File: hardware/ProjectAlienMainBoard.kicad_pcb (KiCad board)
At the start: 2 copper layers, 69.1 x 100.6 mm, 15 parts, among them J1 Bumper Connector, J3 Left Motor Connector, J4 Right Motor Connector, J5 Pixels Connector, J6 Ultrasonic Connector, J7 Micro USB, J8 I2C Multiplexer, U1 4021

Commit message: Updated name to Project A.L.I.E.N. Main Board
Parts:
- moved J5 6.06 mm to (170.2, 135.9)
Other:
- outline, holes or cut-outs redrawn
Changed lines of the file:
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@@
 	)
 	(paper "A4")
+	(title_block
+		(title "A.L.I.E.N. Main Board")
+		(date "2024-08-13")
+		(rev "1.0")
+		(comment 1 "Designed By: Harry Boyd")
+	)
 	(layers
 		(0 "F.Cu" signal)
@@
 		(property ki_fp_filters "Arduino*Nano*")
 		(sheetname "Root")
-		(sheetfile "ProjectAlienArbReplacement.kicad_sch")
+		(sheetfile "ProjectAlienMainBoard.kicad_sch")
 		(attr through_hole)
 		(fp_line
@@
 		(property ki_fp_filters "Connector*:*_1x??_*")
 		(sheetname "Root")
-		(sheetfile "ProjectAlienArbReplacement.kicad_sch")
+		(sheetfile "ProjectAlienMainBoard.kicad_sch")
 		(attr through_hole)
 		(fp_line
@@
 		(property ki_fp_filters "MountingHole*Pad*")
 		(sheetname "Root")
-		(sheetfile "ProjectAlienArbReplacement.kicad_sch")
+		(sheetfile "ProjectAlienMainBoard.kicad_sch")
 		(attr exclude_from_pos_files exclude_from_bom)
 		(fp_circle
@@
 		(property ki_fp_filters "Connector*:*_1x??_*")
 		(sheetname "Root")
-		(sheetfile "ProjectAlienArbReplacement.kicad_sch")
+		(sheetfile "ProjectAlienMainBoard.kicad_sch")
 		(attr through_hole)
 		(fp_line
@@
 		)
 		(sheetname "Root")
-		(sheetfile "ProjectAlienArbReplacement.kicad_sch")
+		(sheetfile "ProjectAlienMainBoard.kicad_sch")
 		(attr through_hole)
 		(fp_line
@@
 		(property ki_fp_filters "MountingHole*Pad*")
 		(sheetname "Root")
-		(sheetfile "ProjectAlienArbReplacement.kicad_sch")
+		(sheetfile "ProjectAlienMainBoard.kicad_sch")
 		(attr exclude_from_pos_files exclude_from_bom)
 		(fp_circle
@@
 		(property ki_fp_filters "MountingHole*Pad*")
 		(sheetname "Root")
-		(sheetfile "ProjectAlienArbReplacement.kicad_sch")
+		(sheetfile "ProjectAlienMainBoard.kicad_sch")
 		(attr exclude_from_pos_files exclude_from_bom)
 		(fp_circle
@@
 		(property ki_fp_filters "DIP*W7.62mm* SOIC*3.9x9.9mm*P1.27mm* TSSOP*4.4x5mm*P0.65mm* SOIC*5.3x10.2mm*P1.27mm*")
 		(sheetname "Root")
-		(sheetfile "ProjectAlienArbReplacement.kicad_sch")
+		(sheetfile "ProjectAlienMainBoard.kicad_sch")
 		(attr through_hole)
 		(fp_line
@@
 	(footprint "Connector_PinHeader_2.54mm:PinHeader_1x03_P2.54mm_Vertical"
 		(layer "F.Cu")
-		(at 164.25 134.62)
+		(at 170.18 135.89)
 		(descr "Through hole straight pin header, 1x03, 2.54mm pitch, single row")
 		(tags "Through hole pin header THT 1x03 2.54mm single row")
@@
 		(property ki_fp_filters "Connector*:*_1x??_*")
 		(sheetname "Root")
-		(sheetfile "ProjectAlienArbReplacement.kicad_sch")
+		(sheetfile "ProjectAlienMainBoard.kicad_sch")
 		(attr through_hole)
 		(fp_line
@@
 		)
 		(sheetname "Root")
-		(sheetfile "ProjectAlienArbReplacement.kicad_sch")
+		(sheetfile "ProjectAlienMainBoard.kicad_sch")
 		(fp_rect
 			(start 13.003859 -11.74657)
@@
 		(property ki_fp_filters "MountingHole*Pad*")
 		(sheetname "Root")
-		(sheetfile "ProjectAlienArbReplacement.kicad_sch")
+		(sheetfile "ProjectAlienMainBoard.kicad_sch")
 		(attr exclude_from_pos_files exclude_from_bom)
 		(fp_circle
@@
 		(property ki_fp_filters "Connector*:*_1x??_*")
 		(sheetname "Root")
-		(sheetfile "ProjectAlienArbReplacement.kicad_sch")
+		(sheetfile "ProjectAlienMainBoard.kicad_sch")
 		(attr through_hole)
 		(fp_line
@@
 		(property ki_fp_filters "Connector*:*_1x??_*")
 		(sheetname "Root")
-		(sheetfile "ProjectAlienArbReplacement.kicad_sch")
+		(sheetfile "ProjectAlienMainBoard.kicad_sch")
 		(attr through_hole)
 		(fp_line
@@
 		(property ki_fp_filters "Connector*:*_1x??_*")
 		(sheetname "Root")
-		(sheetfile "ProjectAlienArbReplacement.kicad_sch")
+		(sheetfile "ProjectAlienMainBoard.kicad_sch")
 		(attr through_hole)
 		(fp_line
@@
 		(property ki_fp_filters "Connector*:*_1x??_*")
 		(sheetname "Root")
-		(sheetfile "ProjectAlienArbReplacement.kicad_sch")
+		(sheetfile "ProjectAlienMainBoard.kicad_sch")
 		(attr through_hole)
 		(fp_line
@@
 		)
 	)
+	(gr_arc
+		(start 173.05 148.5)
+		(mid 171.585534 152.035534)
+		(end 168.05 153.5)
+		(stroke
+			(width 0.05)
+			(type default)
+		)
+		(layer "Edge.Cuts")
+	)
 	(gr_line
-		(start 103.95 52.9)
-		(end 173.05 52.9)
+		(start 173.05 148.5)
+		(end 173.05 57.9)
 		(stroke
 			(width 0.05)
@@
 	)
 	(gr_line
-		(start 103.95 153.5)
-		(end 103.95 52.9)
+		(start 168.05 52.9)
+		(end 108.95 52.9)
 		(stroke
 			(width 0.05)
@@
 	)
 	(gr_line
-		(start 173.05 153.5)
-		(end 173.05 52.9)
+		(start 108.95 153.5)
+		(end 168.05 153.5)
+		(stroke
+			(width 0.05)
+			(type default)
+		)
+		(layer "Edge.Cuts")
+	)
+	(gr_arc
+		(start 108.95 153.5)
+		(mid 105.414466 152.035534)
+		(end 103.95 148.5)
+		(stroke
+			(width 0.05)
+			(type default)
+		)
+		(layer "Edge.Cuts")
+	)
+	(gr_arc
+		(start 168.05 52.9)
+		(mid 171.585534 54.364466)
+		(end 173.05 57.9)
+		(stroke
+			(width 0.05)
+			(type default)
+		)
+		(layer "Edge.Cuts")
+	)
+	(gr_arc
+		(start 103.95 57.9)
+		(mid 105.414466 54.364466)
+		(end 108.95 52.9)
 		(stroke
 			(width 0.05)
@@
 	)
 	(gr_line
-		(start 173.05 153.5)
-		(end 103.95 153.5)
+		(start 103.95 57.9)
+		(end 103.95 148.5)
 		(stroke
 			(width 0.05)
@@
 	)
 	(group ""
-		(members "314df4b6-4d44-4a2c-9948-7561ff2cd3bf" "56a19394-8d3b-494b-8114-4e80be3695e4"
-			"6238faaa-2a80-4400-b16f-04a6e4e532ca" "79eefe5f-d36b-4a34-8db9-96859c714df3"
-			"870ac478-1f87-4e97-96b2-28e8b3a96d61" "c06d917b-8f1b-4ed2-943a-9ff2319c5b92"
-			"c2b0b19a-48aa-4ae2-a952-9f25db60e84b" "d9d95080-6408-4977-b597-9c6bf767d439"
+		(members "0762931e-818e-41e5-9866-3b0bf242c0d1" "50c6c233-3866-4b6d-8cb0-e3d3b624f4dc"
+			"6c16ee7f-4a9d-448a-ad8a-cde8a30f06c7" "72e14dae-e42e-4db7-a5ae-2bd5013e1e8d"
+			"c860c21a-08f5-4c03-8915-206027afa625" "dc3d2b26-e902-4e49-9b06-8b6bc477fa51"
+			"e5c0358d-c8e8-4da7-b468-3a30b2833571" "f5535738-ebcb-4d12-8861-2c8079402787"
 		)
 	)

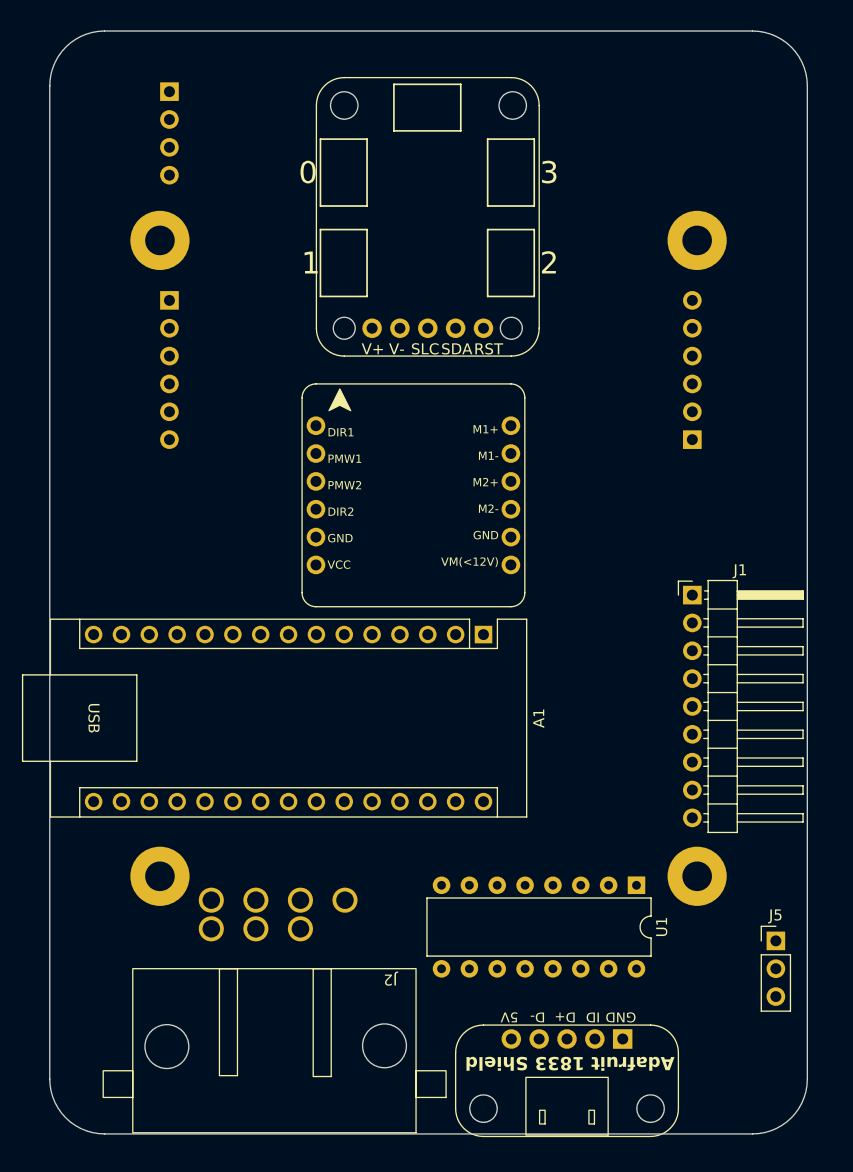
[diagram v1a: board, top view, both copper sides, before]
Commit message: Swapped resistors for SMT
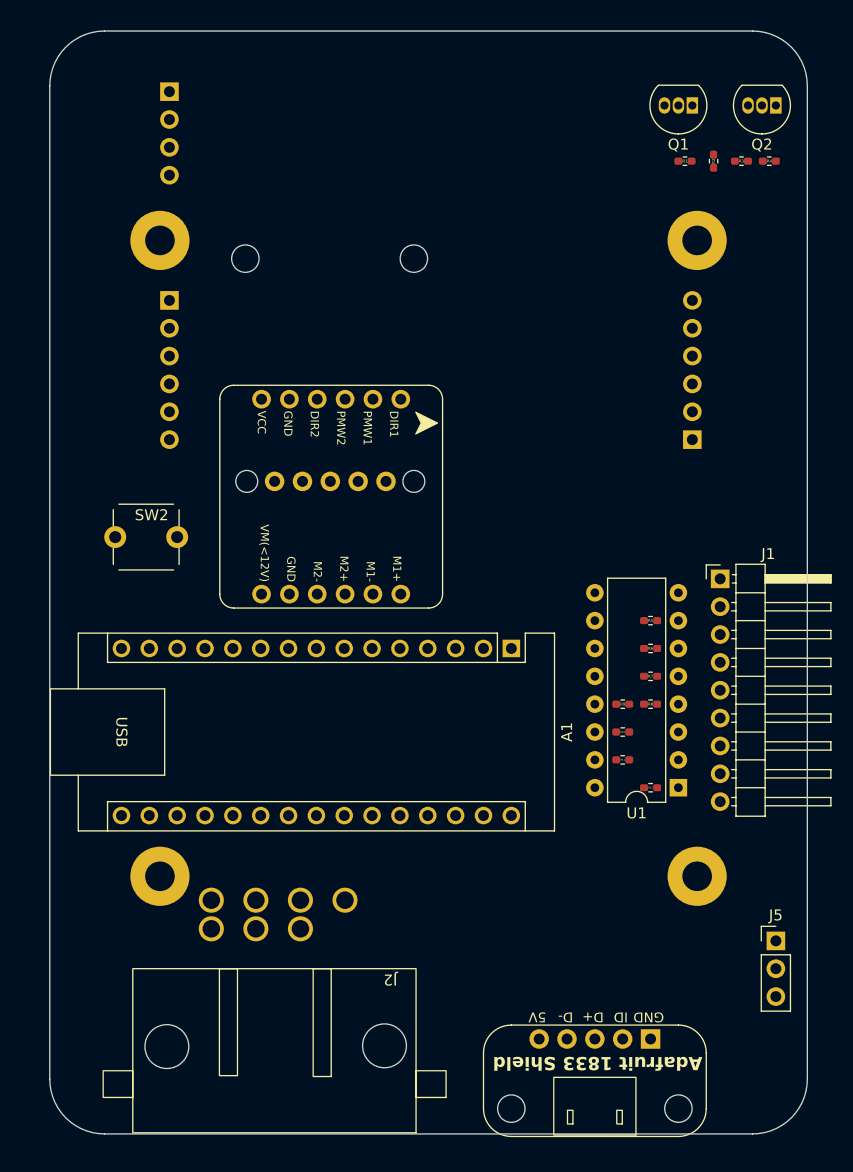
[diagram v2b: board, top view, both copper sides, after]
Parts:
- added Q1: 2N3904, Package_TO_SOT_THT:TO-92_Inline, F.Cu at (162.6, 59.7)
- added Q2: 2N3904, Package_TO_SOT_THT:TO-92_Inline, F.Cu at (170.2, 59.7)
- added R1: 1k, Resistor_SMD:R_0402_1005Metric_Pad0.72x0.64mm_HandSolder, F.Cu at (161.9, 64.8)
- added R10: 10k, Resistor_SMD:R_0402_1005Metric_Pad0.72x0.64mm_HandSolder, F.Cu at (156.2, 116.8)
- added R11: 10k, Resistor_SMD:R_0402_1005Metric_Pad0.72x0.64mm_HandSolder, F.Cu at (156.2, 119.4)
- added R12: 10k, Resistor_SMD:R_0402_1005Metric_Pad0.72x0.64mm_HandSolder, F.Cu at (158.8, 121.9)
- added R2: 1k, Resistor_SMD:R_0402_1005Metric_Pad0.72x0.64mm_HandSolder, F.Cu at (164.5, 64.8)
- added R3: 1k, Resistor_SMD:R_0402_1005Metric_Pad0.72x0.64mm_HandSolder, F.Cu at (167.0, 64.8)
- added R4: 1k, Resistor_SMD:R_0402_1005Metric_Pad0.72x0.64mm_HandSolder, F.Cu at (169.6, 64.8)
- added R5: 10k, Resistor_SMD:R_0402_1005Metric_Pad0.72x0.64mm_HandSolder, F.Cu at (158.8, 106.7)
- added R6: 10k, Resistor_SMD:R_0402_1005Metric_Pad0.72x0.64mm_HandSolder, F.Cu at (158.8, 109.2)
- added R7: 10k, Resistor_SMD:R_0402_1005Metric_Pad0.72x0.64mm_HandSolder, F.Cu at (158.8, 111.8)
- added R8: 10k, Resistor_SMD:R_0402_1005Metric_Pad0.72x0.64mm_HandSolder, F.Cu at (158.8, 114.3)
- added R9: 10k, Resistor_SMD:R_0402_1005Metric_Pad0.72x0.64mm_HandSolder, F.Cu at (156.2, 114.3)
- added SW2: SW_Push, Two_Pin_Through_Hole_Push_Button:Two_Pin_Through_Hole_Push_Button, F.Cu at (112.7, 99.1)
- J8: moved to B.Cu
- moved J8 16.5 mm to (129.6, 84.0), turned to 180 degrees
- moved U1 9.69 mm to (161.3, 121.9), turned to 180 degrees
- moved M1 7.58 mm to (129.6, 95.4), turned to -90 degrees
- moved J1 2.94 mm to (165.1, 102.9)
- moved A1 2.84 mm to (146.1, 109.2)
- moved J7 2.54 mm to (153.7, 148.6)
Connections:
- net Net-(A1-A0) renamed DIR1
- net Net-(A1-A1) renamed DIR2
- net Net-(A1-D10) renamed PWM2
- A1 pad 10: unconnected-(A1-D7-Pad10) -> USONIC_TRIG
- A1 pad 12: Net-(A1-D9) -> PWM1
- A1 pad 17: unconnected-(A1-3V3-Pad17) -> +3.3V
- A1 pad 23: unconnected-(A1-SDA/A4-Pad23) -> I2C_SDA
- A1 pad 24: unconnected-(A1-SCL/A5-Pad24) -> I2C_SCL
- A1 pad 26: unconnected-(A1-A7-Pad26) -> ENC2B
- A1 pad 3: unconnected-(A1-~{RESET}-Pad3) -> Net-(A1-~{RESET}-Pad3)
- A1 pad 30: unconnected-(A1-VIN-Pad30) -> +5V
- A1 pad 5: unconnected-(A1-D2-Pad5) -> ENC1A
- A1 pad 6: unconnected-(A1-D3-Pad6) -> ENC2A
- A1 pad 7: unconnected-(A1-D4-Pad7) -> ENC1B
- A1 pad 8: unconnected-(A1-D5-Pad8) -> PIXELS_DATA_3.3V
- A1 pad 9: unconnected-(A1-D6-Pad9) -> USONIC_ECHO
- J3 pad 1: unconnected-(J3-Pin_1-Pad1) -> GND
- J3 pad 2: unconnected-(J3-Pin_2-Pad2) -> ENC1B
- J3 pad 3: unconnected-(J3-Pin_3-Pad3) -> ENC1A
- J3 pad 4: unconnected-(J3-Pin_4-Pad4) -> +3.3V
- J3 pad 5: unconnected-(J3-Pin_5-Pad5) -> M1-
- J3 pad 6: unconnected-(J3-Pin_6-Pad6) -> M1+
- J4 pad 1: unconnected-(J4-Pin_1-Pad1) -> GND
- J4 pad 2: unconnected-(J4-Pin_2-Pad2) -> ENC2B
- J4 pad 3: unconnected-(J4-Pin_3-Pad3) -> ENC2A
- J4 pad 4: unconnected-(J4-Pin_4-Pad4) -> +3.3V
- J4 pad 5: unconnected-(J4-Pin_5-Pad5) -> M2-
- J4 pad 6: unconnected-(J4-Pin_6-Pad6) -> M2+
- J5 pad 1: unconnected-(J5-Pin_1-Pad1) -> GND
- J5 pad 2: unconnected-(J5-Pin_2-Pad2) -> PIXELS_DATA_5V
- J5 pad 3: unconnected-(J5-Pin_3-Pad3) -> +5V
- J6 pad 1: unconnected-(J6-Pin_1-Pad1) -> GND
- J6 pad 2: unconnected-(J6-Pin_2-Pad2) -> USONIC_ECHO
- J6 pad 3: unconnected-(J6-Pin_3-Pad3) -> USONIC_TRIG
- J6 pad 4: unconnected-(J6-Pin_4-Pad4) -> +5V
- J7 pad 1: unconnected-(J7-Pin_1-Pad1) -> GND
- J7 pad 5: unconnected-(J7-Pin_5-Pad5) -> +5V
- J8 pad 1: unconnected-(J8-Pin_1-Pad1) -> +5V
- J8 pad 2: unconnected-(J8-Pin_2-Pad2) -> GND
- J8 pad 3: unconnected-(J8-Pin_3-Pad3) -> I2C_SCL
- J8 pad 4: unconnected-(J8-Pin_4-Pad4) -> I2C_SDA
- M1 pad 10: unconnected-(M1-M2+-Pad10) -> M2+
- M1 pad 11: unconnected-(M1-M1--Pad11) -> M1-
- M1 pad 12: unconnected-(M1-M1+-Pad12) -> M1+
- M1 pad 2: Net-(A1-D9) -> unconnected-(M1-PMW1-Pad2)
- M1 pad 6: unconnected-(M1-VCC-Pad6) -> +5V
- M1 pad 7: unconnected-(M1-VM(<12V)-Pad7) -> +5V
- M1 pad 9: unconnected-(M1-M2--Pad9) -> M2-

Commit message: Routed Tracks
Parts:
- removed SW2: SW_Push, Two_Pin_Through_Hole_Push_Button:Two_Pin_Through_Hole_Push_Button
- added GND1: GND, TestPoint:TestPoint_Bridge_Pitch2.54mm_Drill0.7mm, F.Cu at (166.4, 149.9)
- added J98: Voltage Breakout, Connector_PinHeader_2.54mm:PinHeader_1x03_P2.54mm_Vertical, F.Cu at (167.6, 139.7)
- added J99: Excess GPIO Pins, Connector_PinHeader_2.54mm:PinHeader_1x03_P2.54mm_Vertical, F.Cu at (109.2, 139.7)
- added SW1: Reset Button, Two_Pin_Through_Hole_Push_Button:Two_Pin_Through_Hole_Push_Button, F.Cu at (109.2, 100.3)
- added TP1: TestPoint, TestPoint:TestPoint_THTPad_D1.0mm_Drill0.5mm, F.Cu at (118.1, 61.0)
- added TP10: TestPoint, TestPoint:TestPoint_THTPad_D1.0mm_Drill0.5mm, F.Cu at (124.4, 88.9)
- added TP11: TestPoint, TestPoint:TestPoint_THTPad_D1.0mm_Drill0.5mm, F.Cu at (124.4, 91.4)
- added TP12: TestPoint, TestPoint:TestPoint_THTPad_D1.0mm_Drill0.5mm, F.Cu at (124.4, 93.9)
- added TP13: TestPoint, TestPoint:TestPoint_THTPad_D1.0mm_Drill0.5mm, F.Cu at (149.8, 86.3)
- added TP14: TestPoint, TestPoint:TestPoint_THTPad_D1.0mm_Drill0.5mm, F.Cu at (149.8, 88.9)
- added TP15: TestPoint, TestPoint:TestPoint_THTPad_D1.0mm_Drill0.5mm, F.Cu at (149.8, 91.4)
- added TP16: TestPoint, TestPoint:TestPoint_THTPad_D1.0mm_Drill0.5mm, F.Cu at (149.8, 93.9)
- added TP17: TestPoint, TestPoint:TestPoint_THTPad_D1.0mm_Drill0.5mm, F.Cu at (118.1, 82.5)
- added TP18: TestPoint, TestPoint:TestPoint_THTPad_D1.0mm_Drill0.5mm, F.Cu at (118.1, 80.0)
- added TP19: TestPoint, TestPoint:TestPoint_THTPad_D1.0mm_Drill0.5mm, F.Cu at (158.8, 86.4)
- added TP2: TestPoint, TestPoint:TestPoint_THTPad_D1.0mm_Drill0.5mm, F.Cu at (118.1, 63.5)
- added TP20: TestPoint, TestPoint:TestPoint_THTPad_D1.0mm_Drill0.5mm, F.Cu at (158.8, 88.9)
- added TP3: TestPoint, TestPoint:TestPoint_THTPad_D1.0mm_Drill0.5mm, F.Cu at (141.3, 130.8)
- added TP4: TestPoint, TestPoint:TestPoint_THTPad_D1.0mm_Drill0.5mm, F.Cu at (156.5, 131.4)
- added TP5: TestPoint, TestPoint:TestPoint_THTPad_D1.0mm_Drill0.5mm, F.Cu at (133.3, 128.3)
- added TP6: TestPoint, TestPoint:TestPoint_THTPad_D1.0mm_Drill0.5mm, F.Cu at (133.3, 130.8)
- added TP7: TestPoint, TestPoint:TestPoint_THTPad_D1.0mm_Drill0.5mm, F.Cu at (133.3, 133.3)
- added TP8: TestPoint, TestPoint:TestPoint_THTPad_D1.0mm_Drill0.5mm, F.Cu at (133.3, 135.9)
- added TP9: TestPoint, TestPoint:TestPoint_THTPad_D1.0mm_Drill0.5mm, F.Cu at (124.4, 86.3)
- A1: value Arduino_Nano_Every -> Arduino_Nano_33_BLE
- J2, J5, J7: moved to B.Cu
- moved Q2 76.2 mm to (153.3, 134.0), turned to 90 degrees
- moved Q1 76.0 mm to (146.4, 134.0), turned to 90 degrees
- moved R1 70.8 mm to (141.9, 132.7)
- moved R3 69.5 mm to (149.5, 132.0), turned to -90 degrees
- moved R2 66.0 mm to (146.4, 128.2), turned to -90 degrees
- moved R4 65.5 mm to (153.3, 128.2), turned to -90 degrees
- moved J8 12.4 mm to (137.1, 93.8), turned to 0 degrees
- moved M1 8.05 mm to (137.2, 92.7), turned to 0 degrees
- moved J5 7.73 mm to (168.9, 128.3), turned to 180 degrees
- moved R10 2.84 mm to (153.7, 115.6)
- moved R11 2.84 mm to (153.7, 118.1)
- moved R9 2.84 mm to (153.7, 113.0)
- moved J1 2.84 mm to (162.6, 101.6)
- moved R5 2.84 mm to (156.2, 105.4)
- moved R7 2.84 mm to (156.2, 110.5)
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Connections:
- A1 pad 14: unconnected-(A1-MOSI-Pad14) -> Buzzer
- A1 pad 15: unconnected-(A1-MISO-Pad15) -> D12
- A1 pad 16: unconnected-(A1-SCK-Pad16) -> D13
- A1 pad 29: Net-(A1-GND-Pad29) -> GND
- A1 pad 4: Net-(A1-GND-Pad29) -> GND
- J1 pad 1: +5V -> +3.3V
- J2 pad 7: +5V -> +3.3V
- M1 pad 2: unconnected-(M1-PMW1-Pad2) -> PWM1
- U1 pad 16: +5V -> +3.3V
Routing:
- net +3.3V: track 0.00 -> 245.1 mm
- net +5V: track 0.00 -> 164.3 mm
- net USONIC_TRIG: track 0.00 -> 68.3 mm
- net USONIC_ECHO: track 0.00 -> 63.0 mm
- net SHIFT_REG_CLOCK: track 0.00 -> 61.0 mm, vias 0 -> 1
- net SHIFT_REG_LOAD: track 0.00 -> 57.7 mm
- net I2C_SDA: track 0.00 -> 49.9 mm
- net ENC2B: track 0.00 -> 49.3 mm
- net PIXELS_DATA_3.3V: track 0.00 -> 48.9 mm
- net DIR1: track 0.00 -> 47.4 mm, vias 0 -> 1
- net M1-: track 0.00 -> 46.8 mm
- net I2C_SCL: track 0.00 -> 44.3 mm
- net M1+: track 0.00 -> 43.4 mm
- net ENC2A: track 0.00 -> 43.3 mm
- net ENC1A: track 0.00 -> 40.3 mm
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
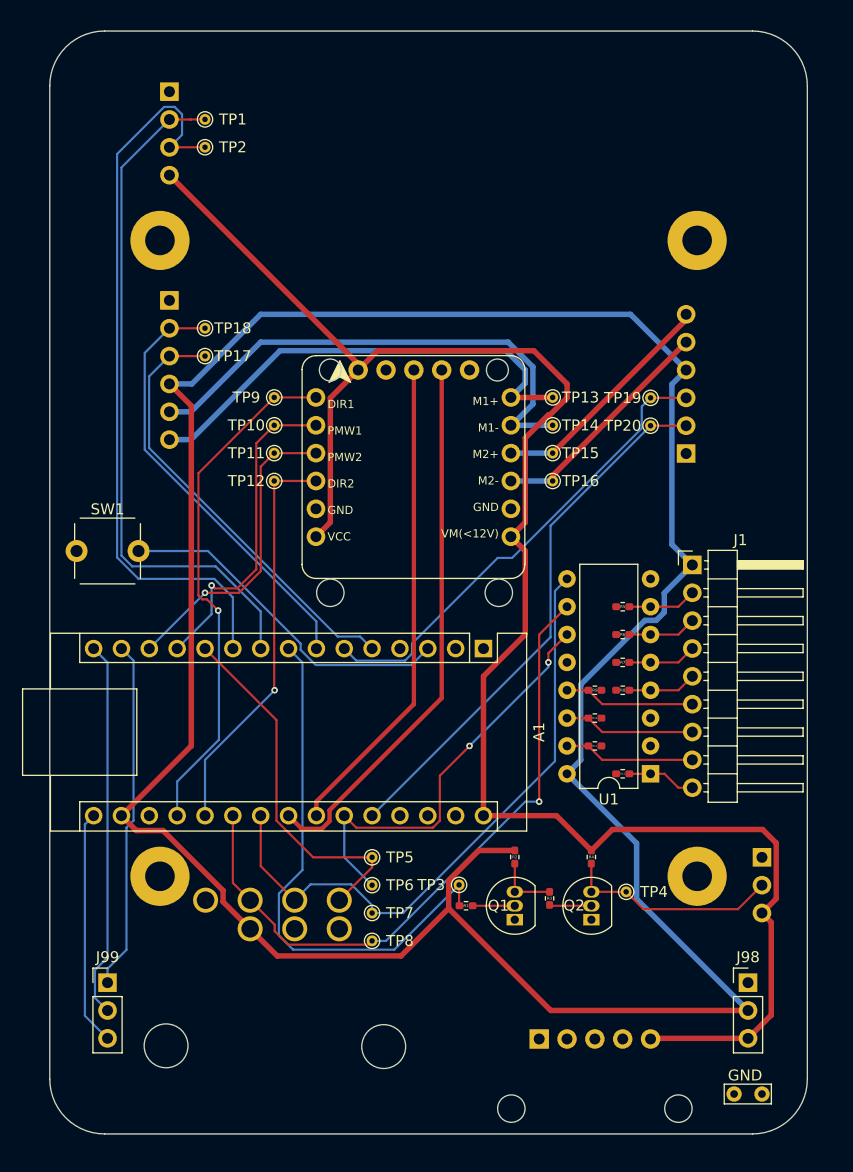
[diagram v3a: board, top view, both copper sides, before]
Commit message: Added ground plane
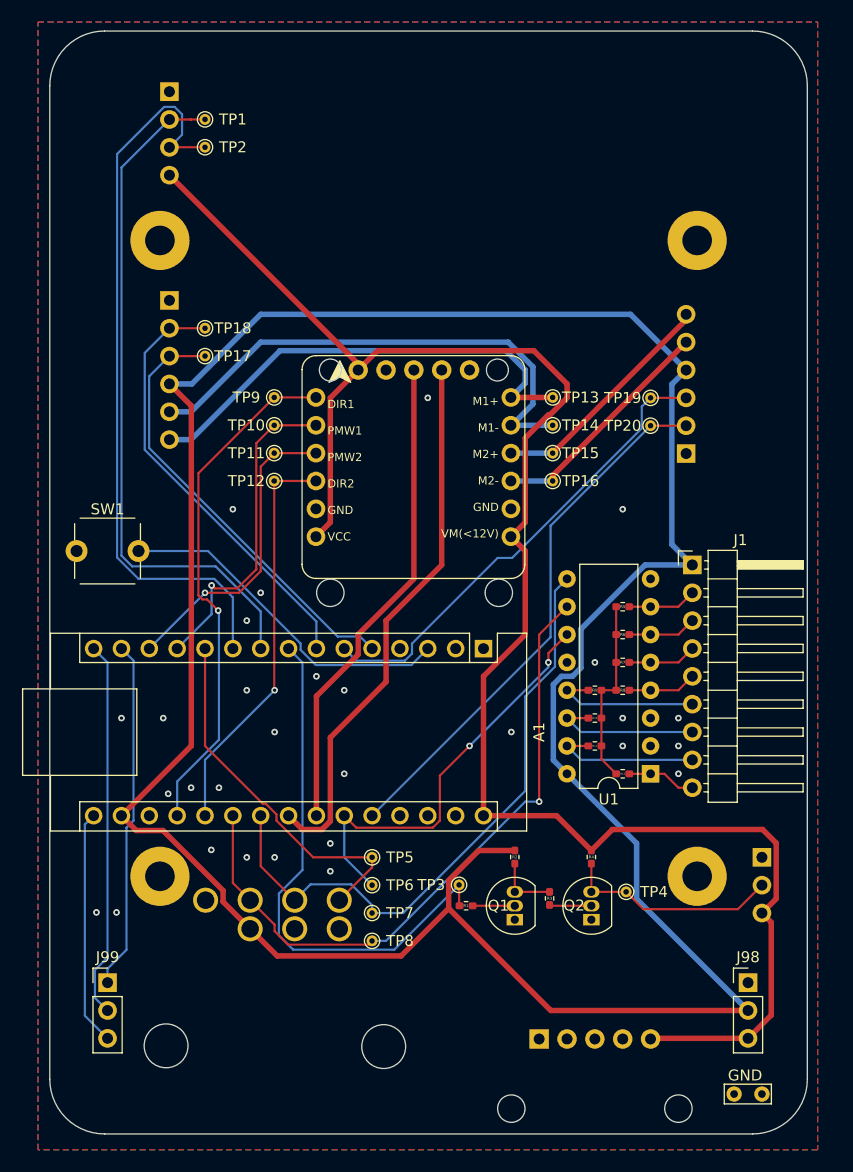
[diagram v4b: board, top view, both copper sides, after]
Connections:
- A1 pad 14: Buzzer -> D11
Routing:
- net GND: track 0.00 -> 17.1 mm, vias 0 -> 29
- net +3.3V: track 245.1 -> 248.6 mm
- net Net-(J1-Pin_7): track 12.0 -> 13.9 mm
- net Net-(J1-Pin_8): track 12.0 -> 13.9 mm
- net Net-(J1-Pin_6): track 12.0 -> 13.9 mm
- added copper zone on B.Cu, net GND
- added copper zone on F.Cu, net GND
